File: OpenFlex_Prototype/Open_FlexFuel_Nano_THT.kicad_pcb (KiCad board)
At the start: 2 copper layers, 111.4 x 69.9 mm, 44 parts, among them J1 Molex MAX150_2x10, J2 Debug_pin_DupontConnector, M3 MountingHole_3.2mm_M3_DIN965_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, Q1 IRF740, Q2 IRF740, Q3 IRF740, Q4 IRF740, U1 LM324, U2 TC4424, U3 TC4424, U4 LM2940S-5.0, U5 ESP32-S2-DEVKITC-1

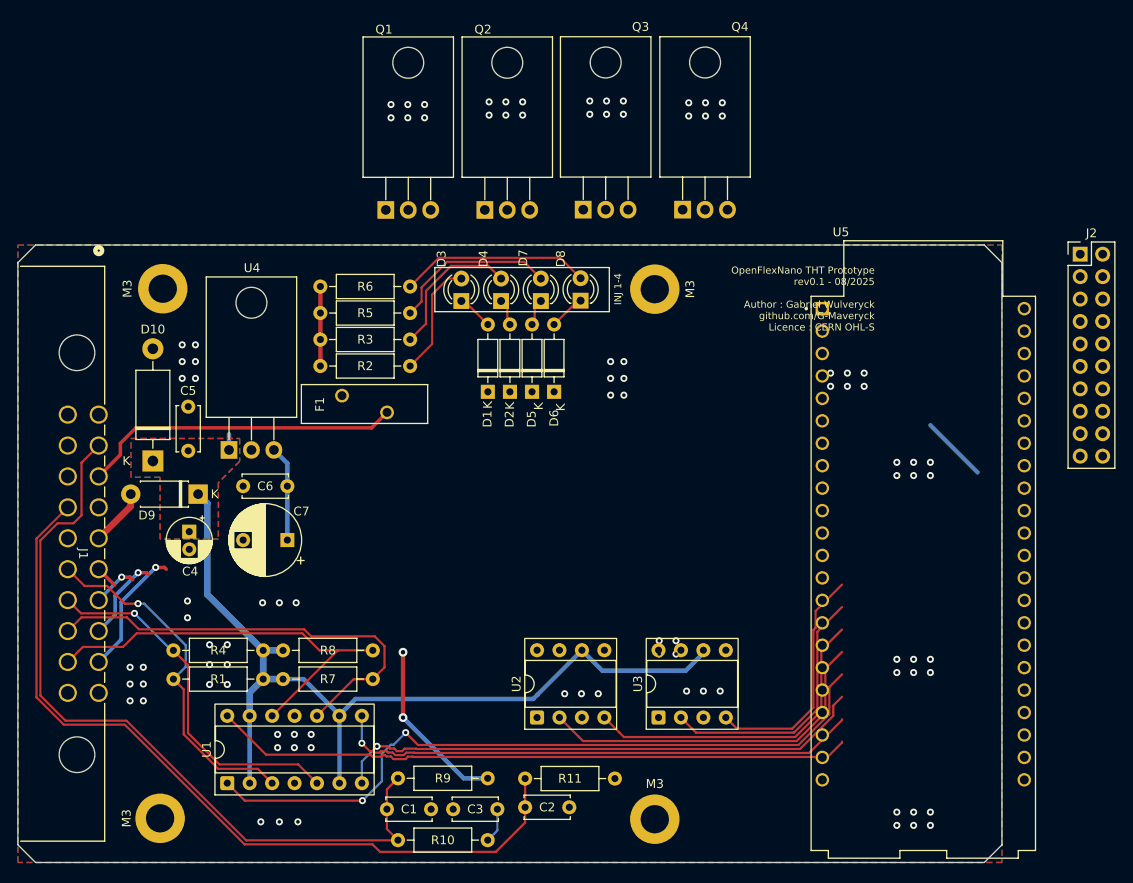
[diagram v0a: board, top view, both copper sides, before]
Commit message: Updated PCB to ESP32-S2-Devkit-C1
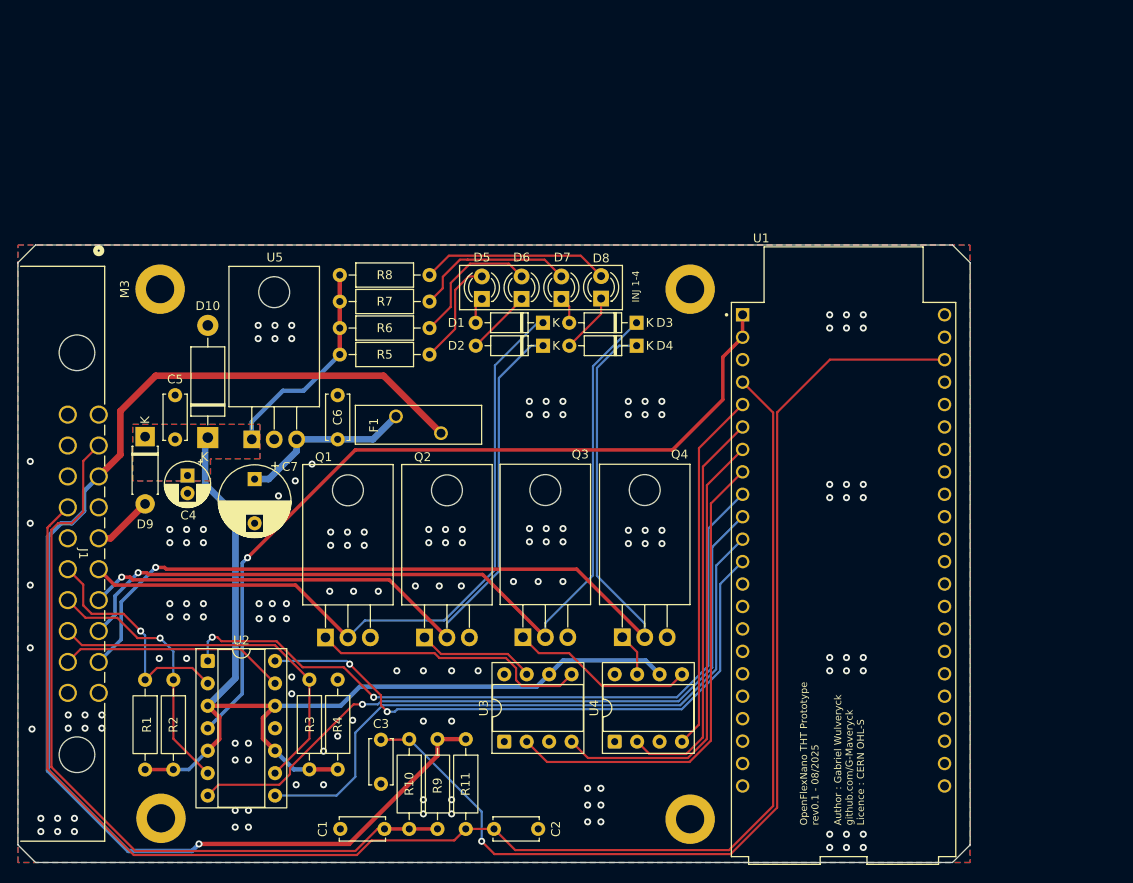
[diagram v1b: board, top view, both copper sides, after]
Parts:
- removed J2: Debug_pin_DupontConnector, Connector_PinHeader_2.54mm:PinHeader_2x10_P2.54mm_Vertical
- removed the R7 at (188.8, 94.4)
- removed the R8 at (188.8, 91.2)
- removed the U1 at (172.3, 106.2)
- added R2: 10k, Resistor_THT:R_Axial_DIN0207_L6.3mm_D2.5mm_P10.16mm_Horizontal, F.Cu at (166.2, 94.5)
- added R3: 10k, Resistor_THT:R_Axial_DIN0207_L6.3mm_D2.5mm_P10.16mm_Horizontal, F.Cu at (181.6, 94.5)
- added U4: TC4424, Package_DIP:DIP-8_W7.62mm_Socket, F.Cu at (216.2, 101.5)
- U2: value TC4424 -> LM324; footprint Package_DIP:DIP-8_W7.62mm_Socket -> Package_DIP:DIP-14_W7.62mm_Socket
- moved Q1 48.9 mm to (183.4, 89.7)
- moved Q2 48.9 mm to (194.6, 89.7)
- moved Q3 48.9 mm to (205.8, 89.7)
- moved Q4 48.9 mm to (217.0, 89.7)
- moved U2 37.8 mm to (170.1, 92.4), turned to 0 degrees
- moved R4 18.9 mm to (184.8, 94.5), turned to -90 degrees
- moved U3 17.7 mm to (203.7, 101.5)
- moved R11 17.5 mm to (199.3, 101.2), turned to -90 degrees
- moved C3 15.3 mm to (189.7, 101.3), turned to -90 degrees
- moved R10 14.5 mm to (192.9, 101.2), turned to -90 degrees
- moved D3 14.2 mm to (218.6, 54.1), turned to 180 degrees
- moved D4 10.7 mm to (218.6, 56.7), turned to 180 degrees
- moved D1 10.0 mm to (208.0, 54.1), turned to 180 degrees
- moved U1 9.05 mm to (242.1, 83.2)
- moved D9 8.85 mm to (163.0, 67.0), turned to -90 degrees
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- renumbered D5 to D3, D6 to D4, D3 to D5, D4 to D6, R2 to R5, R3 to R6, R5 to R7, R6 to R8, U5 to U1, U4 to U5
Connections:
- J1 pad 3: +5V -> VDDA
- R4 pad 1: /Connector/INJ_CH2 -> /Connector/INJ_CH4
- U1 pad J1_1: unconnected-(U5-3V3_J1_1-PadJ1_1) -> VSS
- U1 pad J1_2: unconnected-(U5-3V3_J1_2-PadJ1_2) -> VSS
- U1 pad J1_20: VDD -> unconnected-(U1-GPIO14-PadJ1_20)
- U2 pad 1: unconnected-(U2-NC-Pad1) -> /IO_Drivers/INJ_SIGNAL_CH1
- U2 pad 2: /IO_Drivers/MCU_INJ2 -> /Connector/INJ_CH1
- U2 pad 3: GND -> +12V
- U2 pad 4: /IO_Drivers/MCU_INJ1 -> VSS
- U2 pad 5: Net-(Q1-G) -> +12V
- U2 pad 6: +12V -> /Connector/INJ_CH2
- U2 pad 7: Net-(Q2-G) -> /IO_Drivers/INJ_SIGNAL_CH2
- U2 pad 8: unconnected-(U2-NC-Pad8) -> /IO_Drivers/INJ_SIGNAL_CH3
- U3 pad 2: /IO_Drivers/MCU_INJ4 -> /IO_Drivers/MCU_INJ2
- U3 pad 4: /IO_Drivers/MCU_INJ3 -> /IO_Drivers/MCU_INJ1
- U3 pad 5: Net-(Q3-G) -> Net-(Q1-G)
- U3 pad 7: Net-(Q4-G) -> Net-(Q2-G)
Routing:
- net VDDA: track 19.8 -> 143.0 mm, vias 2 -> 1
- net /IO_Drivers/Temp_Signal: track 4.53 -> 120.6 mm, vias 0 -> 1
- net /Connector/INJ_DRIVE_CH4: track 14.7 -> 110.3 mm
- net VSS: track 0.00 -> 92.9 mm, vias 0 -> 1
- net /Connector/INJ_DRIVE_CH3: track 9.72 -> 97.4 mm
- net /Connector/INJ_DRIVE_CH1: track 2.55 -> 81.8 mm
- net /Connector/Flex_snsr_SIGN: track 91.9 -> 170.4 mm
- net /Connector/INJ_DRIVE_CH2: track 5.05 -> 81.7 mm
- net +5V: track 36.5 -> 0.00 mm
- net Net-(Q1-G): track 0.00 -> 31.5 mm
- net +12V: track 114.1 -> 139.7 mm
- net /Connector/INJ_CH4: track 47.2 -> 25.7 mm
- net /IO_Drivers/INJ_SIGNAL_CH2: track 61.0 -> 82.0 mm
- net Net-(Q3-G): track 0.00 -> 20.8 mm
- net /IO_Drivers/INJ_SIGNAL_CH3: track 59.9 -> 74.8 mm, vias 1 -> 0
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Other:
- board size 111.4 x 69.9 mm -> 107.8 x 69.9 mm

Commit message: Updated and sourced EmulatoBoard (DevBoard)
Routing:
- net GND: vias 146 -> 156

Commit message: Updated Sourcing for prototype
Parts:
- F1: footprint Fuse:Fuse_BelFuse_0ZRE0055FF_L14.0mm_W4.1mm -> Fuse:Fuse_BelFuse_0ZRE0005FF_L8.3mm_W3.8mm
- moved R5 10.2 mm to (185.0, 58.0), turned to 0 degrees
- moved R6 10.2 mm to (185.0, 54.9), turned to 0 degrees
- moved F1 6.72 mm to (191.6, 62.0), turned to -90 degrees
- moved R3 3.20 mm to (184.8, 94.5)
- moved R4 3.20 mm to (181.6, 94.5)
- moved R7 0.11 mm to (185.0, 51.8)
- moved U4 0.06 mm to (216.1, 101.5)
- renumbered J1 to J2
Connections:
- R5 pad 1: Net-(D5-A) -> +12V
- R5 pad 2: +12V -> Net-(D5-A)
- R6 pad 1: Net-(D6-A) -> +12V
- R6 pad 2: +12V -> Net-(D6-A)
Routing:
- net VDDA: track 143.0 -> 136.1 mm
- net VDD: track 19.7 -> 17.3 mm
- net GND: vias 156 -> 171

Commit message: Enclosure WIP
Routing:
- net GND: vias 171 -> 174
